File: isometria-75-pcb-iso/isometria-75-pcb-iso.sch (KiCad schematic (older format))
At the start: 32 parts, among them J101 USB, J102 SPI, J103 Conn_01x01_Male, Q101 AO3400A, SW101 RST, SW102 BOOT, U101 XC6206P332MR, U102 STM32F072CBTx

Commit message: changed regulator symbol to submodule
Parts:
- U101: symbol Regulator_Linear:XC6206PxxxMR -> kicad-keyboard-parts:XC6206PxxxMR-Regulator_Linear
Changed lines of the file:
@@
 EESchema Schematic File Version 4
+LIBS:isometria-75-pcb-iso-cache
 EELAYER 30 0
 EELAYER END
@@
 $EndComp
 $Comp
-L Regulator_Linear:XC6206PxxxMR U101
+L kicad-keyboard-parts:XC6206PxxxMR-Regulator_Linear U101
 U 1 1 5E63D7AB
 P 2800 2300

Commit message: fixed minor bugs, migrated to new libs
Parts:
- removed R102: 10R, Resistor_SMD:R_0402_1005Metric, symbol Device:R_Small
- added R2: 10k, Resistor_SMD:R_0402_1005Metric, symbol Device:R_Small
- SW1: renamed from SW101; footprint random-keyboard-parts:SKQG-1155865 -> Button_Switch_SMD:SW_SPST_SKQG_WithStem
- SW2: renamed from SW102; footprint random-keyboard-parts:SKQG-1155865 -> Button_Switch_SMD:SW_SPST_SKQG_WithStem
- renumbered C101 to C1, C110 to C10, C111 to C11, C112 to C12, C113 to C13, C114 to C14, C115 to C15, C116 to C16, C117 to C17, C102 to C2, C103 to C3, C104 to C4, C105 to C5, C106 to C6, C107 to C7, C108 to C8, C109 to C9, J101 to J1, J102 to J2, J103 to J3, Q101 to Q1, R101 to R1, R103 to R3, R104 to R4, R105 to R5, R106 to R6, R107 to R7, U101 to U1, U102 to U2
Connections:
- net +3V3: now also C14.1, U2.9 (VDDA)
- net GND: now also R2.2
- net LED_PWM: now also R2.1
- net VDDA: no longer C14.1, U2.9 (VDDA)

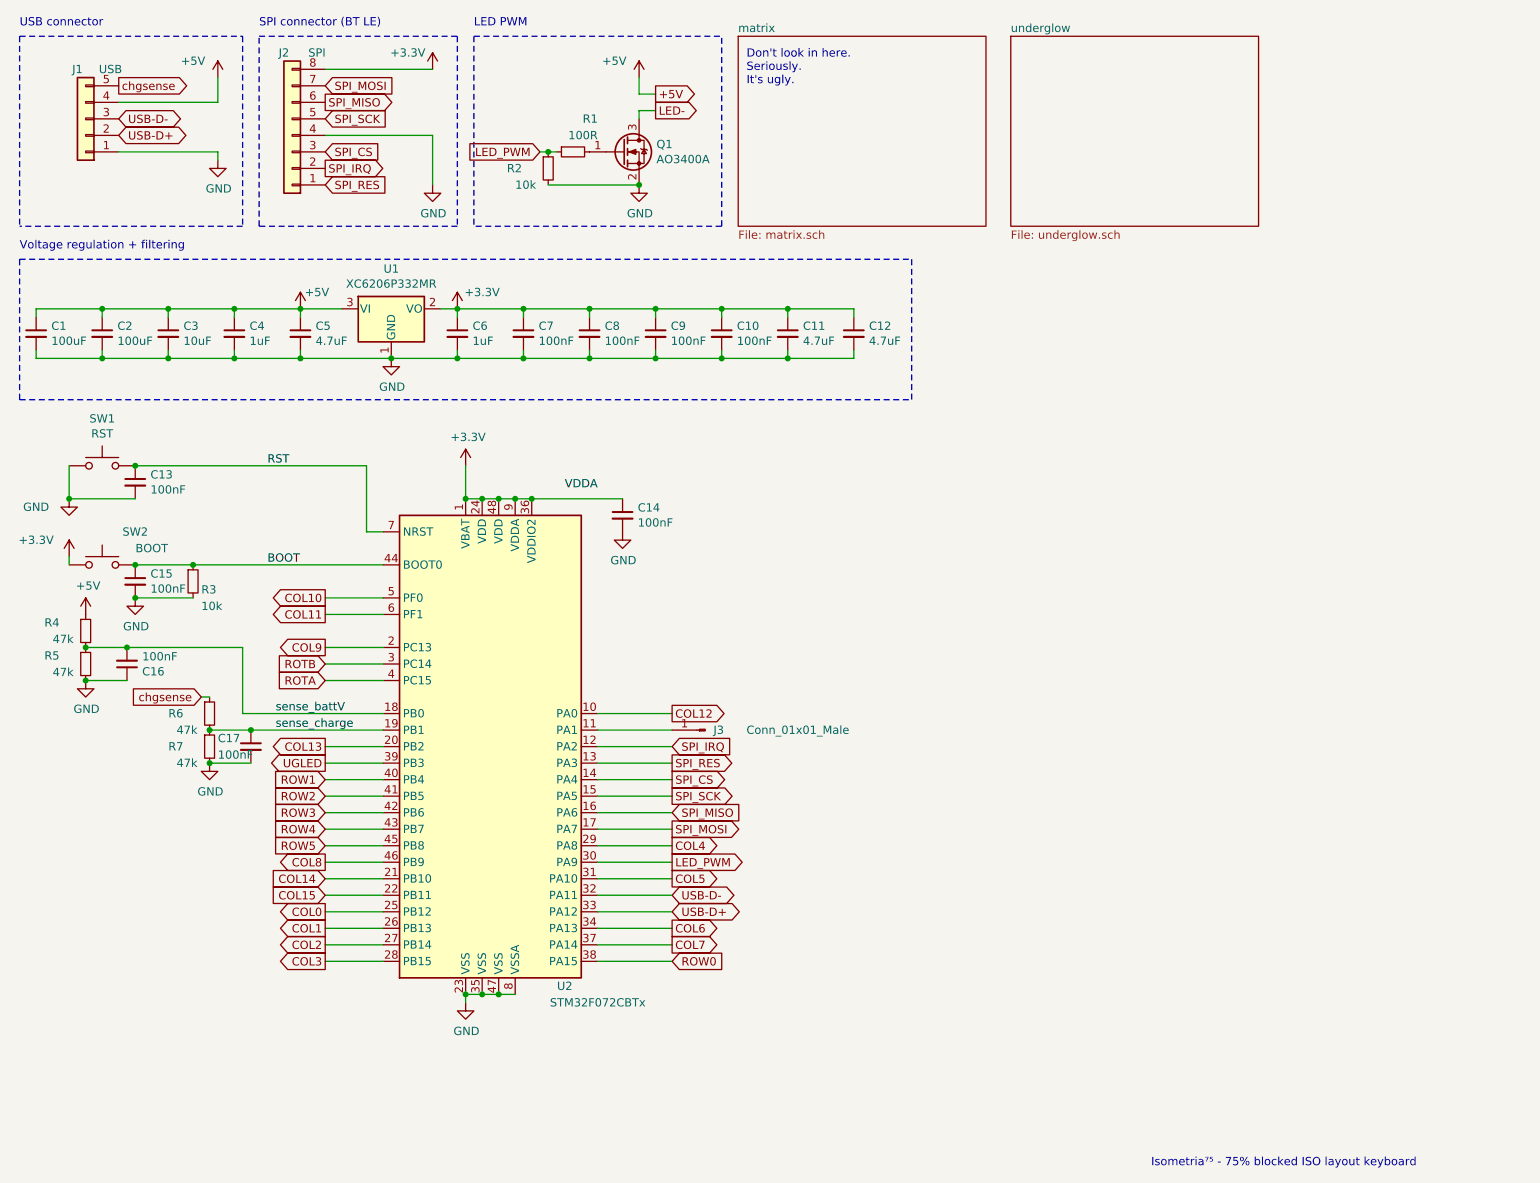
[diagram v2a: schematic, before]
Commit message: started nRF v2 rework
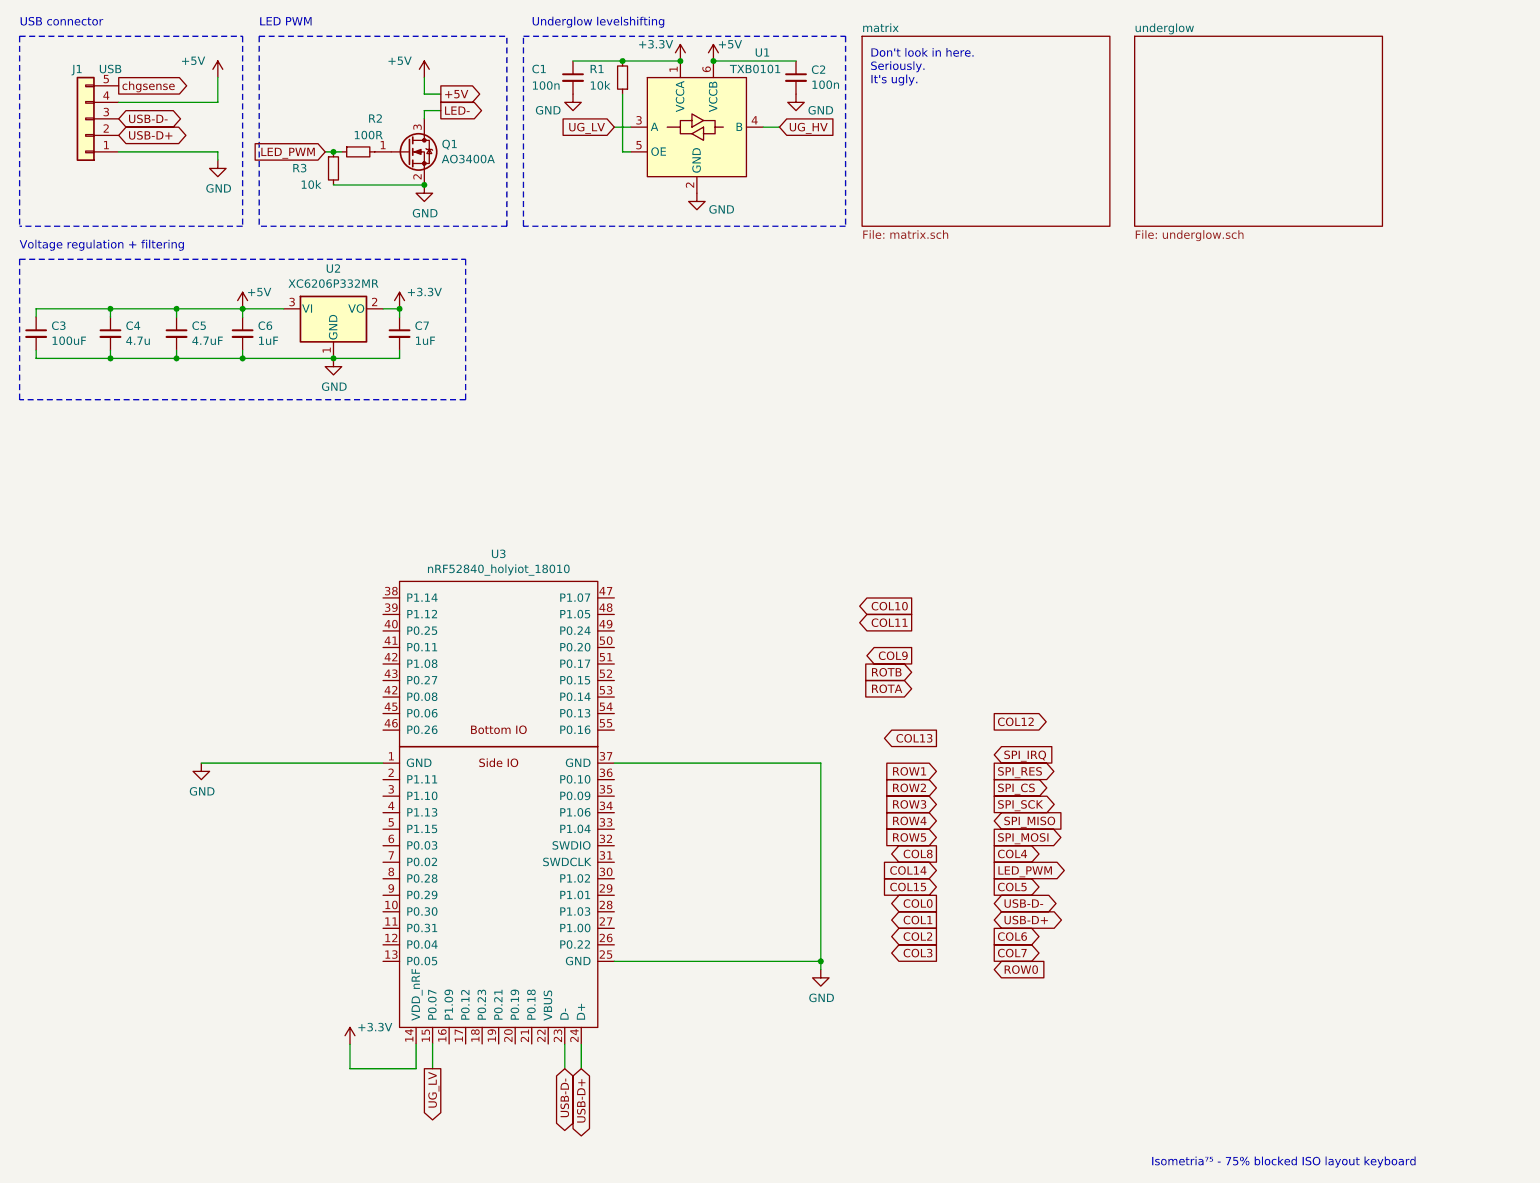
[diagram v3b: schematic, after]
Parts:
- removed C10, C13, C14, C15, C16, C17, C7, C8, C9: 100nF, Capacitor_SMD:C_0402_1005Metric, symbol Device:C_Small
- removed C11, C12: 4.7uF, Capacitor_SMD:C_0402_1005Metric, symbol Device:C_Small
- removed J2: SPI, Connector_JST:JST_SH_SM08B-SRSS-TB_1x08-1MP_P1.00mm_Horizontal, symbol Connector_Generic:Conn_01x08
- removed J3: Conn_01x01_Male, Connector_PinHeader_2.54mm:PinHeader_1x01_P2.54mm_Vertical, symbol Connector:Conn_01x01_Male
- removed R3: 10k, Resistor_SMD:R_0402_1005Metric, symbol Device:R_Small
- removed R4, R5, R6, R7: 47k, Resistor_SMD:R_0402_1005Metric, symbol Device:R_Small
- removed SW1: RST, Button_Switch_SMD:SW_SPST_SKQG_WithStem, symbol Switch:SW_Push
- removed SW2: BOOT, Button_Switch_SMD:SW_SPST_SKQG_WithStem, symbol Switch:SW_Push
- removed U2: STM32F072CBTx, Package_QFP:LQFP-48_7x7mm_P0.5mm, symbol MCU_ST_STM32F0:STM32F072CBTx
- added C1: 100n, Capacitor_SMD:C_0603_1608Metric_Pad1.05x0.95mm_HandSolder, symbol Device:C_Small
- added R1: 10k, Resistor_SMD:R_0603_1608Metric_Pad1.05x0.95mm_HandSolder, symbol Device:R_Small
- added U1: TXB0101, Package_TO_SOT_SMD:SOT-363_SC-70-6, symbol kicad-keyboard-parts:TXB0101
- added U3: nRF52840_holyiot_18010, kicad-keyboard-parts:nRF52840_holyiot_18010, symbol kicad-keyboard-parts:nRF52840_holyiot_18010
- C2: value 100uF -> 100n; footprint Capacitor_Tantalum_SMD:CP_EIA-3528-21_Kemet-B -> Capacitor_SMD:C_0603_1608Metric_Pad1.05x0.95mm_HandSolder; LCSC C16133 -> (none)
- C4: renamed from C3; value 10uF -> 4.7u; footprint Capacitor_Tantalum_SMD:CP_EIA-3216-18_Kemet-A -> Capacitor_SMD:C_0603_1608Metric_Pad1.05x0.95mm_HandSolder
- C5: footprint Capacitor_SMD:C_0402_1005Metric -> Capacitor_SMD:C_0603_1608Metric_Pad1.05x0.95mm_HandSolder
- C6: renamed from C4; footprint Capacitor_SMD:C_0402_1005Metric -> Capacitor_SMD:C_0603_1608Metric_Pad1.05x0.95mm_HandSolder
- C7: renamed from C6; footprint Capacitor_SMD:C_0402_1005Metric -> Capacitor_SMD:C_0603_1608Metric_Pad1.05x0.95mm_HandSolder
- R2: renamed from R1; footprint Resistor_SMD:R_0402_1005Metric -> Resistor_SMD:R_0603_1608Metric_Pad1.05x0.95mm_HandSolder
- R3: renamed from R2; footprint Resistor_SMD:R_0402_1005Metric -> Resistor_SMD:R_0603_1608Metric_Pad1.05x0.95mm_HandSolder
- renumbered C1 to C3, U1 to U2
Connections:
- net +3V3: now also C1.1, R1.2, U1.1 (VCCA), U3.14 (VDD_nRF)
- net +5V: now also U1.6 (VCCB)
- net GND: now also C1.2, U1.2 (GND), U3.1 (GND), U3.25 (GND), U3.37 (GND)
- net USB-D+: now also U3.24 (D+)
- net USB-D-: now also U3.23 (D-)
- new net: R1.1, U1.5 (OE)
- new net UG_HV: U1.4 (B)
- new net UG_LV: U1.3 (A), U3.15 (P0.07)
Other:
- note added: "Underglow levelshifting"
- note removed: "SPI connector (BT LE)"
- moved on the sheet: C4, C5, C6, C7, Q1, R2, R3, U2
